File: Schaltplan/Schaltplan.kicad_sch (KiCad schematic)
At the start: 13 parts, among them J1 Conn_01x02_Pin, Q1 IRLZ44N, Q2 IRLZ44N

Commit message: Plan changes
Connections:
- net at A1.4 (GND), BT1.2 (-), Q1.2 (D)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: now also A1.5 (D2); no longer A1.2 (D0/RX)
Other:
- moved on the sheet: A1, BT1, BT2, J1, Q1, Q2, R1, R2, R3, R4, R5, R6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

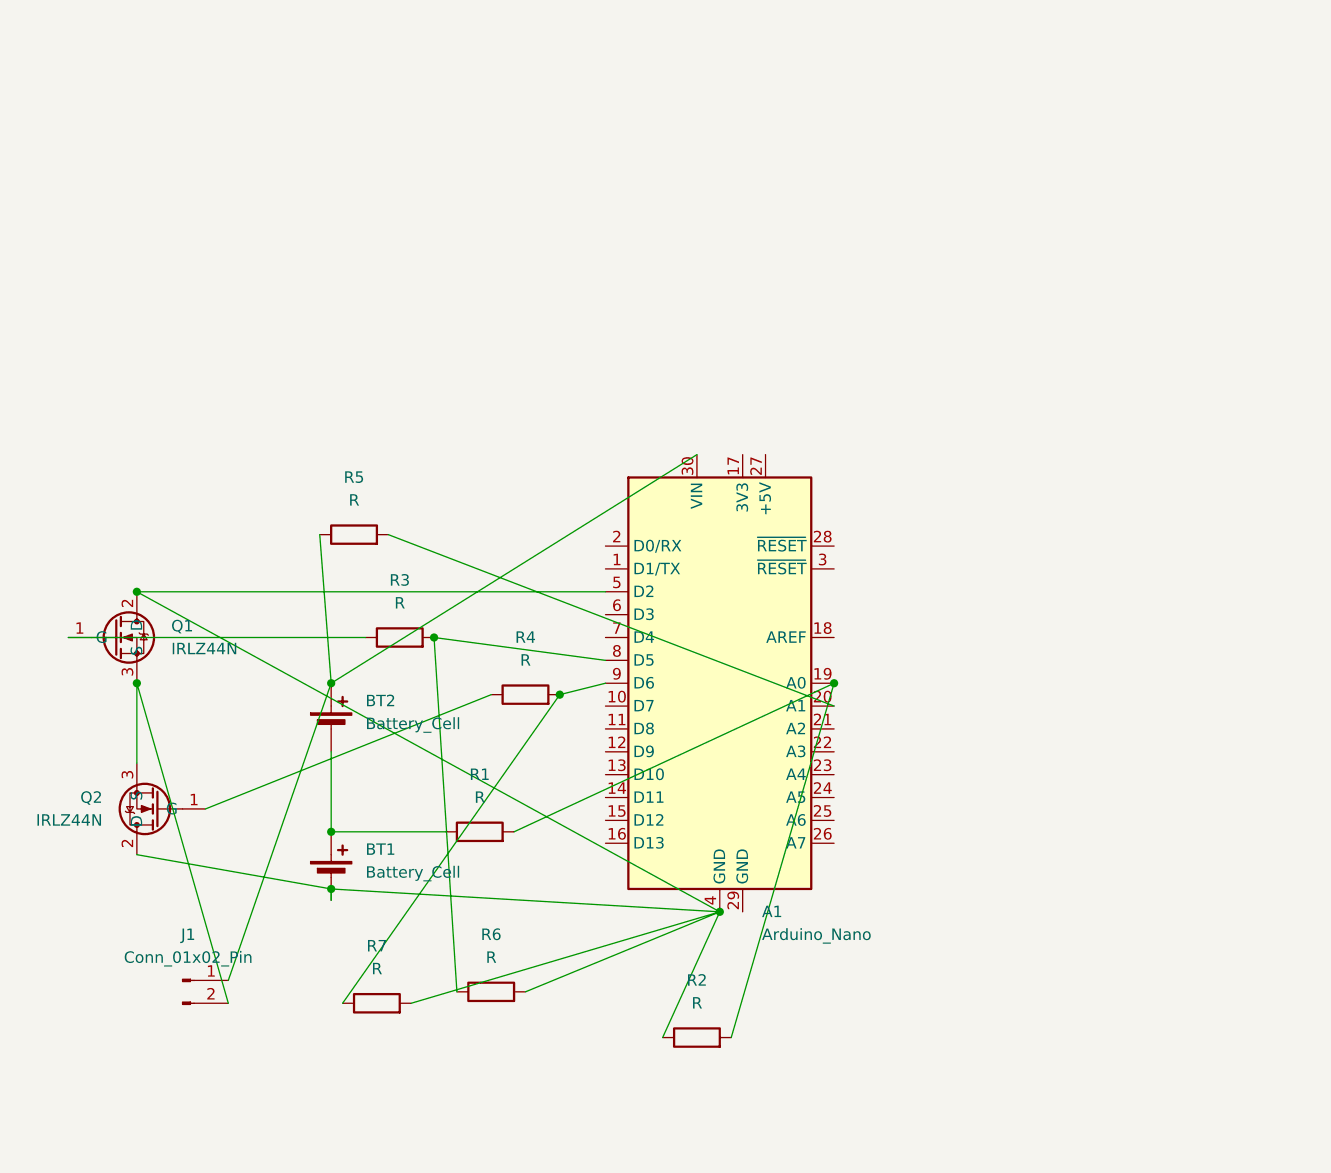
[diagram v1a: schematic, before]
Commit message: Add ACS712 current sensor and update schematic layout
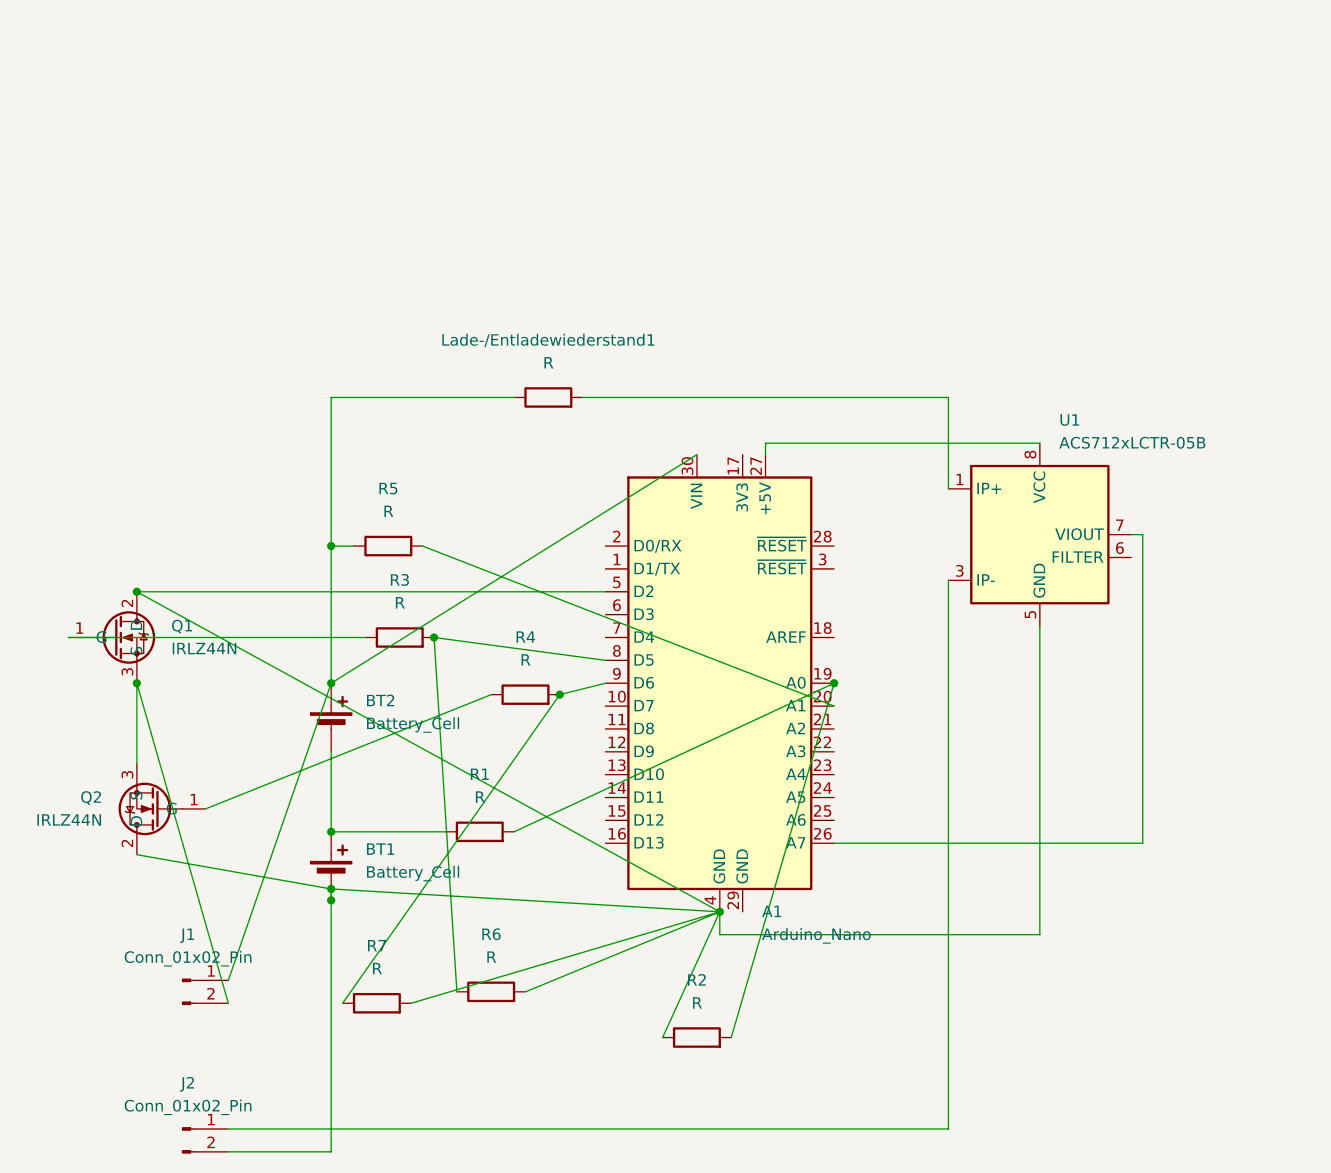
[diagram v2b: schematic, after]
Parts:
- added J2: Conn_01x02_Pin, symbol Connector:Conn_01x02_Pin
- added Lade-/Entladewiederstand1: R, symbol Device:R
- added U1: ACS712xLCTR-05B, Package_SO:SOIC-8_3.9x4.9mm_P1.27mm, symbol Sensor_Current:ACS712xLCTR-05B
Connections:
- net at A1.4 (GND), A1.5 (D2), BT1.2 (-)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: now also J2.2 (Pin_2), U1.5 (GND)
- net at A1.30 (VIN), BT2.1 (+), J1.1 (Pin_1)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: now also Lade-/Entladewiederstand1.1
- net at A1.26 (A7): now also U1.7 (VIOUT)
- net at A1.27 (+5V): now also U1.8 (VCC)
- new net: Lade-/Entladewiederstand1.2, U1.1 (IP+), U1.2 (IP+)
- new net: J2.1 (Pin_1), U1.3 (IP-), U1.4 (IP-)
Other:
- moved on the sheet: R5
